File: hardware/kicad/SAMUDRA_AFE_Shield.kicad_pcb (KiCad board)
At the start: 2 copper layers, 70 x 54 mm, 58 parts, among them CN5 PinHeader_1x10_P2.54mm_Vertic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, CN6 PinHeader_1x08_P2.54mm_Vertic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, CN7 PinHeader_1x06_P2.54mm_Vertic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, J1 TerminalBlock_Phoenix_MKDS-1,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, J2 BNC_Amphenol_B6252HB-NPP3G-50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, SW1 SW_Slide_1P2T_CK_OS102011MS2Q, U1 SOIC-8_3.9x4.9mm_P1.27mm, U2 SOIC-8_3.9x4.9mm_P1.27mm

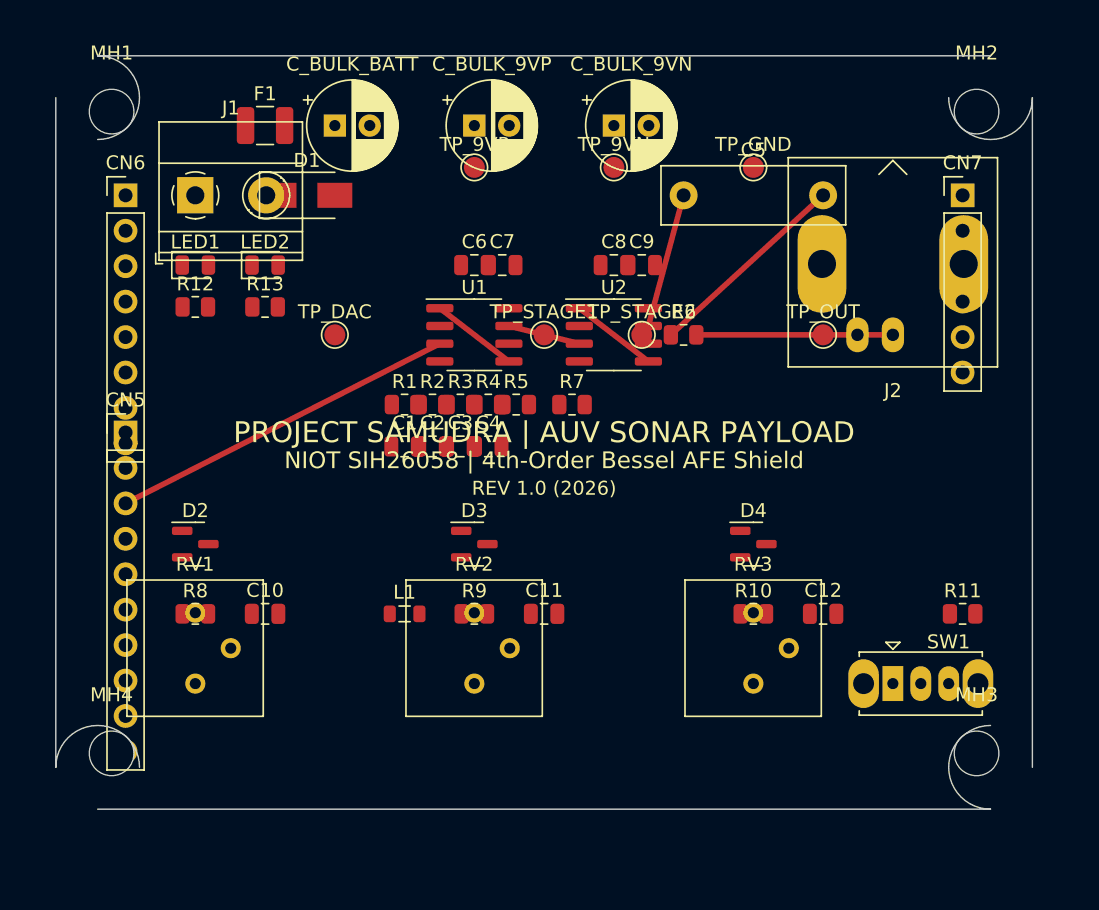
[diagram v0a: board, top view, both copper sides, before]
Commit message: Fix board spacing by laying components out in an 8x7 grid
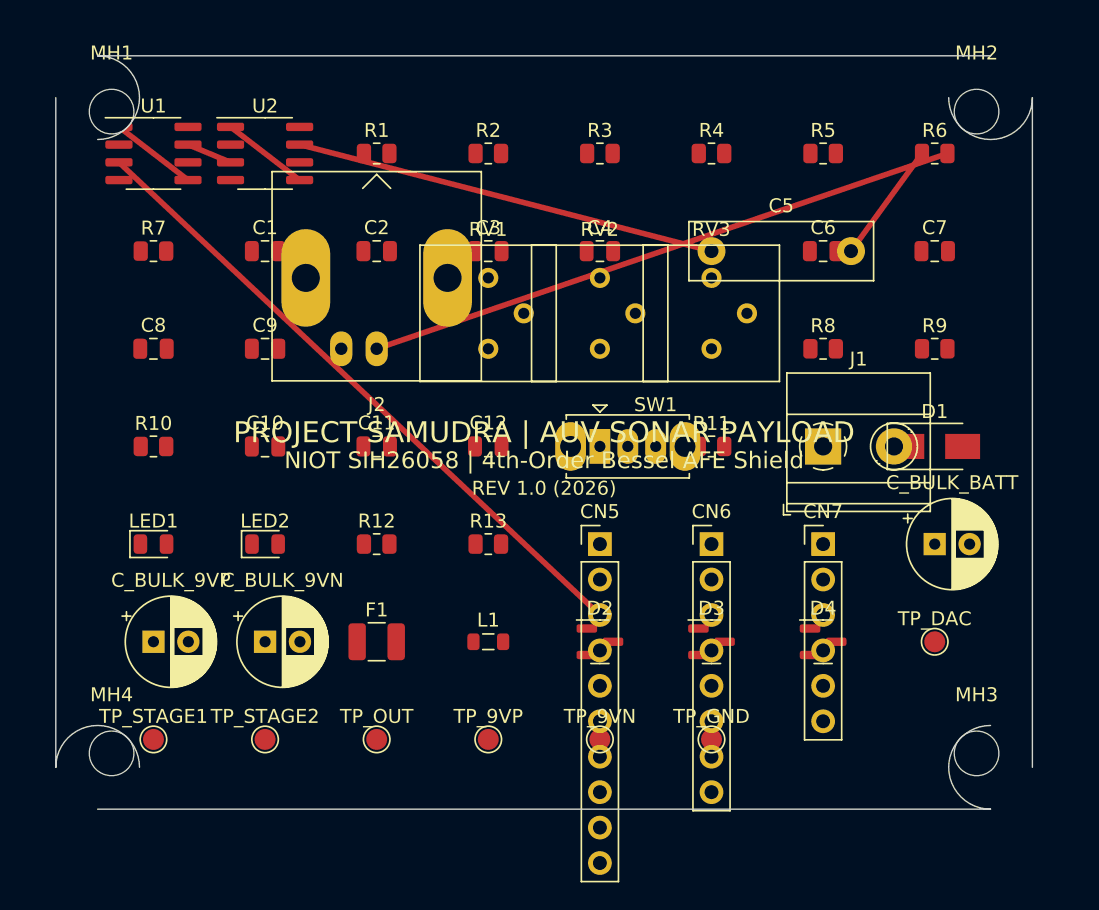
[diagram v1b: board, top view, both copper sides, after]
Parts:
- moved C_BULK_BATT 52.4 mm to (63.0, 35.0)
- moved CN6 48.9 mm to (47.0, 35.0)
- moved R8 48.8 mm to (55.0, 21.0)
- moved D1 48.5 mm to (63.0, 28.0)
- moved J1 48.5 mm to (55.0, 28.0)
- moved TP_DAC 48.3 mm to (63.0, 42.0)
- moved C_BULK_9VN 44.7 mm to (15.0, 42.0)
- moved R10 44.6 mm to (7.00, 28.0)
- moved C_BULK_9VP 43.6 mm to (7.00, 42.0)
- moved TP_OUT 43.2 mm to (23.0, 49.0)
- moved TP_GND 41.1 mm to (47.0, 49.0)
- moved TP_9VN 41.0 mm to (39.0, 49.0)
- moved TP_9VP 41.0 mm to (31.0, 49.0)
- moved TP_STAGE1 40.3 mm to (7.00, 49.0)
- moved TP_STAGE2 39.6 mm to (15.0, 49.0)
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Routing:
- net R6_OUT: track 14.1 -> 43.2 mm
- net PA4: track 25.3 -> 47.3 mm
- net U2B_OUT: track 9.70 -> 30.5 mm
- net C5_OUT: track 14.8 -> 8.65 mm
- net U1B_OUT: track 5.21 -> 3.30 mm

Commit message: Update PCB footprint spacing to minimum 8mm
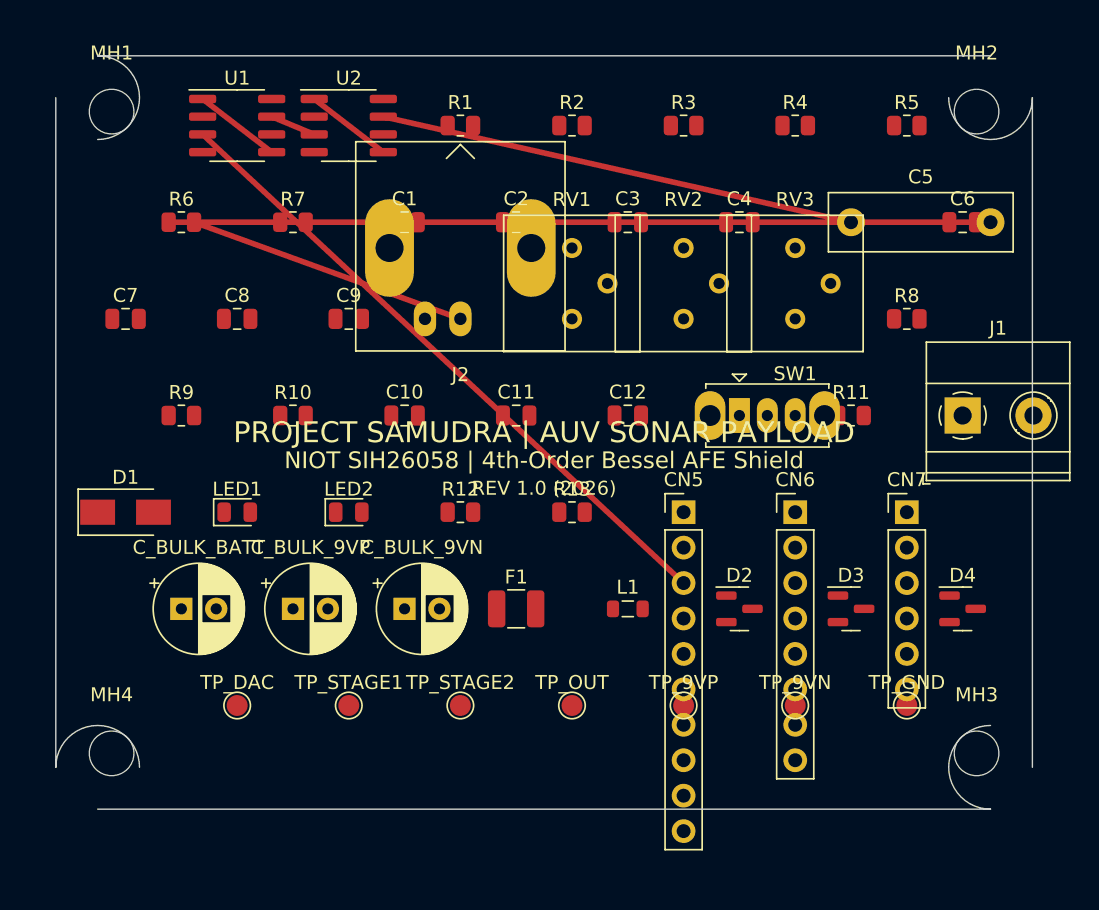
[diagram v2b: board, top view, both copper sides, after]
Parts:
- moved C7 58.2 mm to (5.00, 18.9)
- moved D1 58.2 mm to (5.00, 32.7)
- moved R6 54.2 mm to (9.00, 11.9)
- moved R9 54.2 mm to (9.00, 25.8)
- moved C_BULK_BATT 54.2 mm to (9.00, 39.6)
- moved TP_DAC 50.2 mm to (13.0, 46.6)
- moved TP_9VN 14.2 mm to (53.0, 46.6)
- moved TP_9VP 14.2 mm to (45.0, 46.6)
- moved TP_GND 14.2 mm to (61.0, 46.6)
- moved TP_OUT 14.2 mm to (37.0, 46.6)
- moved TP_STAGE1 14.2 mm to (21.0, 46.6)
- moved TP_STAGE2 14.2 mm to (29.0, 46.6)
- moved C_BULK_9VN 10.3 mm to (25.0, 39.6)
- moved C_BULK_9VP 10.3 mm to (17.0, 39.6)
- moved D2 10.3 mm to (49.0, 39.6)
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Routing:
- net C5_OUT: track 8.65 -> 58.9 mm
- net R6_OUT: track 43.2 -> 20.3 mm
- net U2B_OUT: track 30.5 -> 34.4 mm

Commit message: Fix DRC errors: Add GND zone and offset silkscreen references
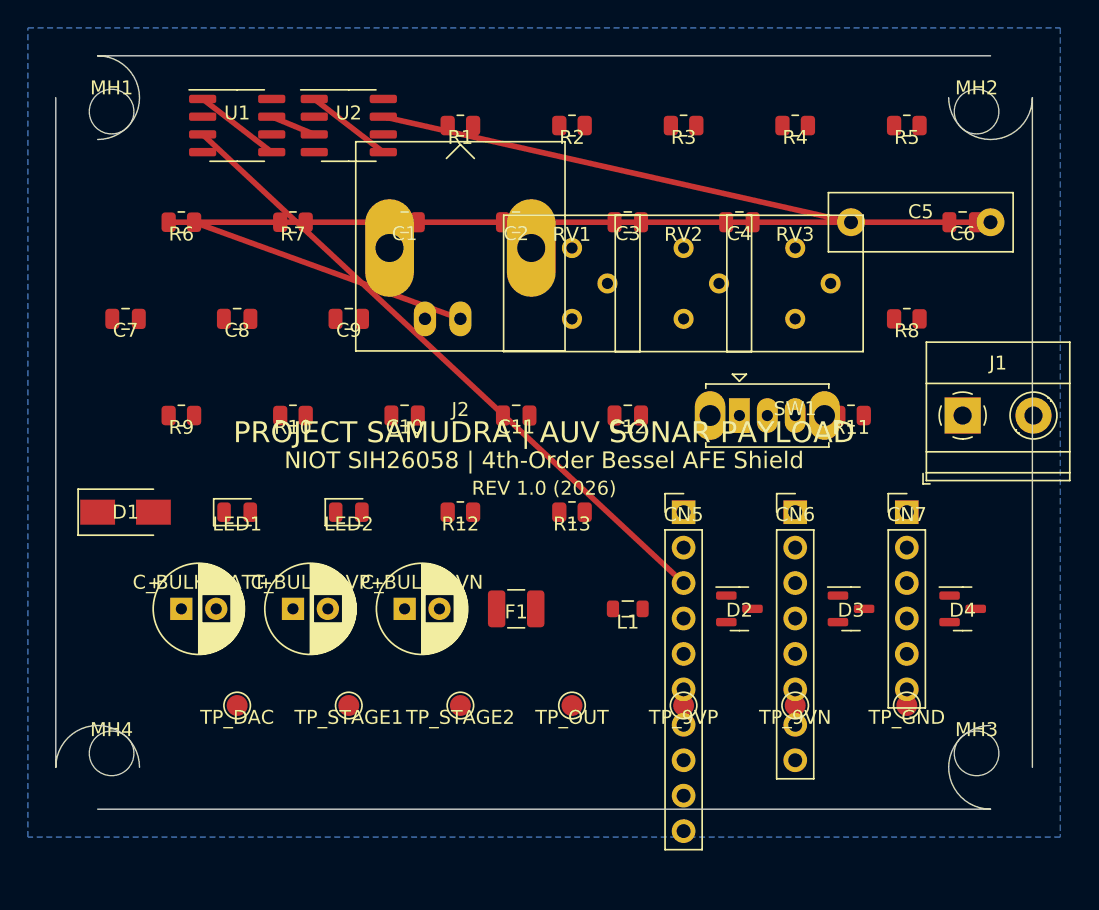
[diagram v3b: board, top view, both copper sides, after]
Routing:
- added copper zone on B.Cu, net GND
